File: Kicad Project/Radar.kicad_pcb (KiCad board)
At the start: 2 copper layers, 30 parts

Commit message: PCB Changes
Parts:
- added C12: C, Capacitors_SMD:C_0603, F.Cu at (160.2, 135.0)
- added C13: C, Capacitors_SMD:C_0603, F.Cu at (160.2, 140.0)
- added C14: C, Capacitors_SMD:C_0603, F.Cu at (163.5, 135.0)
- added R15: R, Resistors_SMD:R_0603, F.Cu at (163.5, 140.0)
- added U1: GALI-1+, RadarComponents:Amplifier, F.Cu at (150.4, 155.2)
- added U10: GALI-2+, RadarComponents:Amplifier, F.Cu at (150.9, 139.6)
- added U6: GALI-2+, RadarComponents:Amplifier, F.Cu at (112.1, 93.8)
- added U8: GALI-2+, RadarComponents:Amplifier, F.Cu at (152.9, 93.5)
- moved R7 68.9 mm to (117.9, 90.8), turned to 90 degrees
- moved .1uF1 67.1 mm to (105.7, 92.6), turned to 180 degrees
- moved R8 64.7 mm to (118.0, 84.6), turned to 270 degrees
- moved R10 54.5 mm to (128.3, 96.6), turned to 270 degrees
- moved C8 54.3 mm to (118.6, 88.1), turned to 180 degrees
- moved R9 51.9 mm to (125.3, 92.6), turned to 180 degrees
- moved C4 50.0 mm to (242.7, 113.1)
- moved R6 50.0 mm to (256.7, 113.0)
- moved C1 50.0 mm to (252.7, 113.1)
- moved C6 50.0 mm to (219.9, 118.1)
- moved C7 50.0 mm to (211.7, 113.1)
- moved R150 50.0 mm to (217.9, 131.8)
- moved R4 50.0 mm to (246.8, 118.1)
- moved R5 50.0 mm to (250.4, 118.1)
- moved C10 50.0 mm to (214.2, 131.8)
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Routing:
- added copper zone on F.Cu, net (none)
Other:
- board outline added: 104.1 x 101.6 mm

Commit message: PCB and Schematic updates
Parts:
- added R16: 75, RadarComponents:100PAD, F.Cu at (240.7, 109.0)
- added R17: 75, RadarComponents:100PAD, F.Cu at (227.9, 123.2)
- added R18: 75, RadarComponents:100PAD, F.Cu at (237.4, 114.1)
- added R19: 75, RadarComponents:100PAD, F.Cu at (220.7, 121.1)
- added U2: MCA1-85L+, RadarComponents:DZ885, F.Cu at (140.9, 118.0)
- added U3: LMV751, RadarComponents:SOT23-5, F.Cu at (125.8, 112.8)
- added U4: LMV751, RadarComponents:SOT23-5, F.Cu at (112.8, 111.1)
- added U5: LMV751, RadarComponents:SOT23-5, F.Cu at (103.9, 111.7)
- added U7: RMK-3-93+, RadarComponents:TT1224, F.Cu at (135.4, 93.4)
- added U9: LEE-39+, RadarComponents:Amplifier, F.Cu at (227.9, 113.7)
- .1uF1, .1uF2, .1uF3, .1uF4, C1, C10, C11, C12, C13, C14, C2, C3, C4, C5, C6, C7, C8, C9: footprint Capacitors_SMD:C_0603 -> RadarComponents:100PAD
- R1, R10, R11, R12, R13, R14, R15, R2, R7, R8, R9: footprint Resistors_SMD:R_0603 -> RadarComponents:100PAD
- moved R6 151.6 mm to (105.2, 117.2)
- moved R5 136.7 mm to (113.7, 117.4)
- moved R4 125.4 mm to (121.5, 112.9)
- moved C4 107.9 mm to (134.8, 111.2), turned to 90 degrees
- moved R3 98.3 mm to (132.1, 118.5)
- moved C1 84.4 mm to (168.3, 111.4), turned to 90 degrees
- moved R2 73.6 mm to (147.3, 105.4), turned to 0 degrees
- moved C3 71.0 mm to (148.6, 115.4), turned to 0 degrees
- moved C2 70.6 mm to (146.8, 109.5), turned to 0 degrees
- moved R1 64.1 mm to (152.8, 112.3)
- moved U1 41.8 mm to (160.3, 114.6), turned to 180 degrees
- moved C11 36.8 mm to (235.7, 104.7)
- moved C7 32.8 mm to (237.4, 133.4)
- moved C5 27.2 mm to (223.2, 137.3)
- moved R150 23.6 mm to (237.9, 119.1)
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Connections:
- net Net-(.1uF4-Pad1) renamed /SourceModule.sch/PowerSplitter
- net Net-(C10-Pad2) renamed /TXRX Module/receive_out
- net Net-(C11-Pad2) renamed /TXRX Module/transmit_in
- C12 pad 1: Net-(C12-Pad1) -> GND
- C13 pad 2: Net-(C13-Pad2) -> GND
- R1 pad 2: Net-(R1-Pad2) -> Net-(C3-Pad2)
- U10 pad 1: Net-(U10-Pad1) -> Net-(C11-Pad1)
- U10 pad 2: Net-(U10-Pad2) -> GND
- U10 pad 3: Net-(U10-Pad3) -> Net-(C14-Pad2)
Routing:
- added copper zone on F.Cu, net /SourceModule.sch/PowerSplitter
- removed copper zone on F.Cu, net (none)

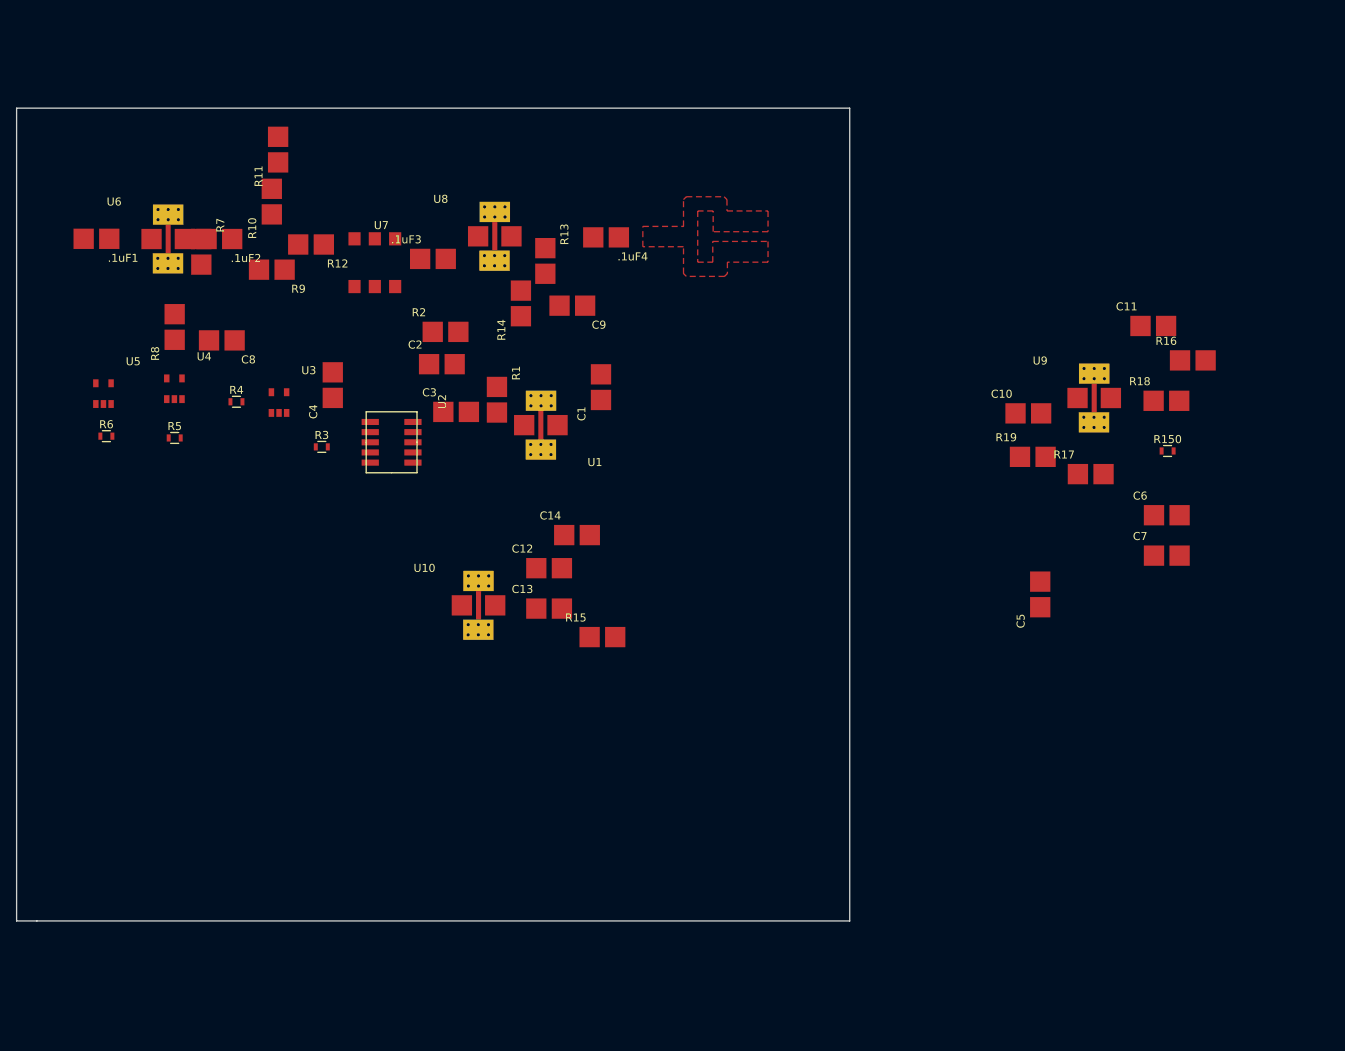
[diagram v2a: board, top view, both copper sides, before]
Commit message: PCB for source Module mostly complete, missing filter. Power Spliter still has issues.
Some minor changes made to all schematics for the net lists to be properall connected

A bunch of parts made
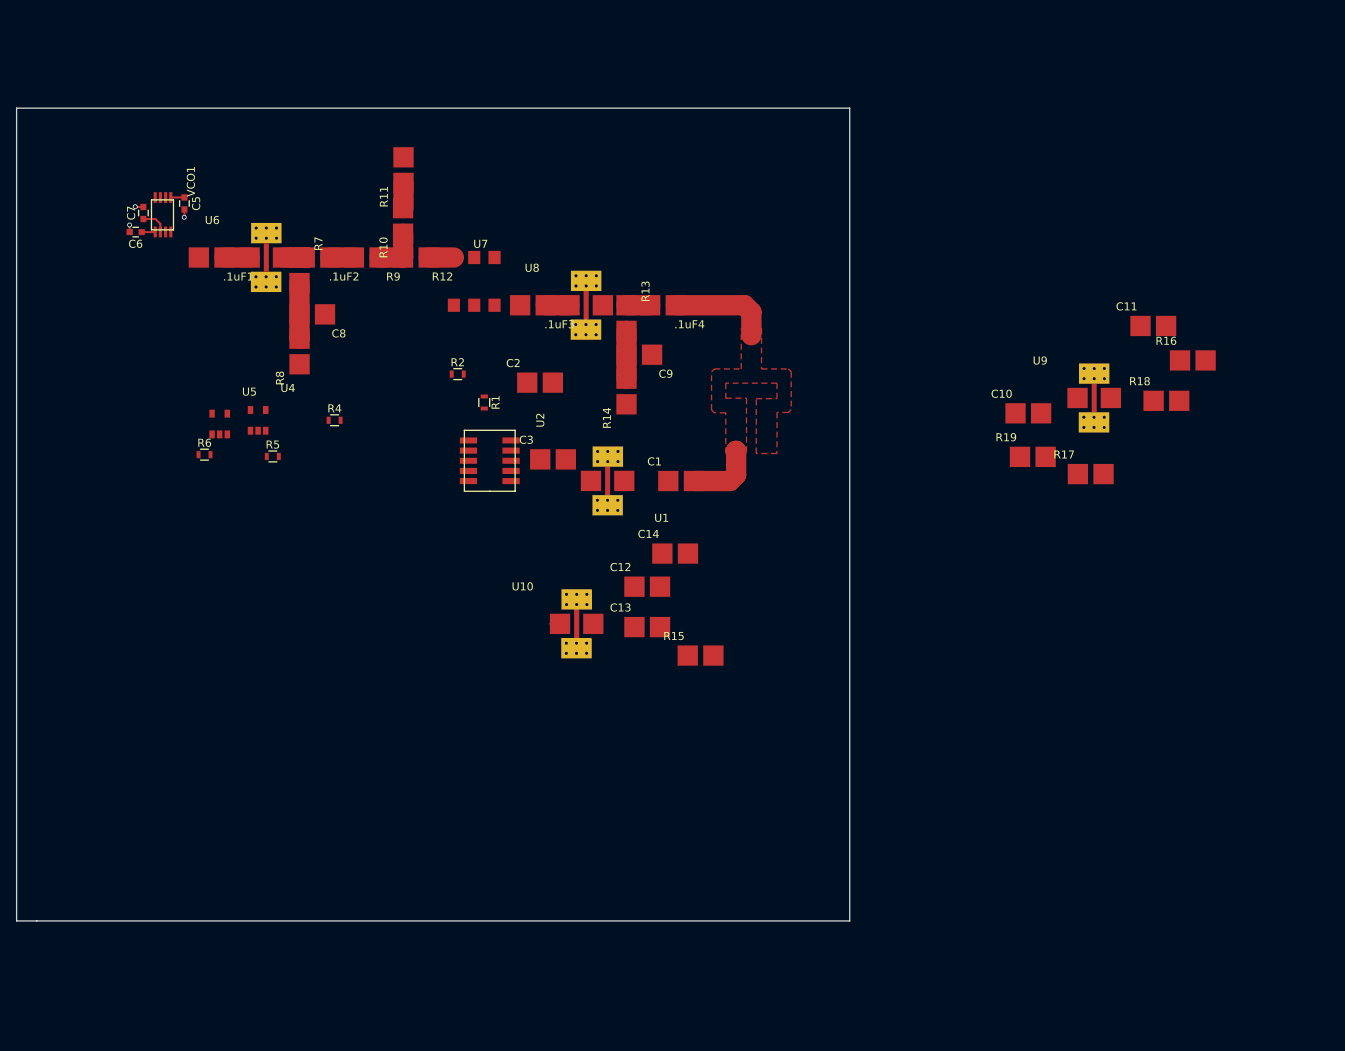
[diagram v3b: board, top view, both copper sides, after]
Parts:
- removed C4: 270pF, RadarComponents:100PAD
- removed R150: R, Resistors_SMD:R_0603
- removed R3: 390k, Resistors_SMD:R_0603
- removed U3: LMV751, RadarComponents:SOT23-5
- added VCO1: MAX2752, RadarComponents:MAX2752, F.Cu at (112.1, 88.2)
- C5, C6, C7: footprint RadarComponents:100PAD -> Capacitors_SMD:C_0603
- R1, R2: footprint RadarComponents:100PAD -> Resistors_SMD:R_0603
- moved C7 135.0 mm to (109.8, 89.3), turned to 90 degrees
- moved C6 133.7 mm to (108.9, 91.7), turned to 180 degrees
- moved C5 118.9 mm to (115.0, 88.1), turned to 270 degrees
- moved R14 17.2 mm to (171.5, 112.0)
- moved R10 16.6 mm to (143.6, 90.6)
- moved R8 15.9 mm to (130.6, 106.9)
- moved R11 15.9 mm to (143.6, 84.3)
- moved C1 15.2 mm to (176.7, 124.1), turned to 0 degrees
- moved U5 15.0 mm to (118.4, 115.5)
- moved .1uF1 14.6 mm to (118.7, 93.6)
- moved U8 14.3 mm to (164.4, 102.1)
- moved .1uF3 13.6 mm to (158.9, 99.6), turned to 180 degrees
- moved C3 13.5 mm to (160.7, 121.4)
- moved R12 13.2 mm to (144.2, 93.6)
- moved U7 12.6 mm to (147.9, 95.7)
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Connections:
- .1uF4 pad 1: /SourceModule.sch/PowerSplitter -> /DownconverterPreampModule/LO
- C1 pad 2: Net-(C1-Pad2) -> /DownconverterPreampModule/LO
- C10 pad 2: /TXRX Module/receive_out -> /DownconverterPreampModule/RFIN
- C11 pad 2: /TXRX Module/transmit_in -> /DownconverterPreampModule/LO
- R1 pad 2: Net-(C3-Pad2) -> Net-(R1-Pad2)
- R13 pad 2: Net-(R13-Pad2) -> Net-(C9-Pad2)
- R14 pad 2: Net-(R13-Pad2) -> Net-(C9-Pad2)
- U2 pad 3: Net-(R3-Pad2) -> Net-(R4-Pad2)
- U2 pad 5: Net-(U2-Pad5) -> /DownconverterPreampModule/RFIN
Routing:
- net /DownconverterPreampModule/LO: track 0.00 -> 21.3 mm
- net Net-(C8-Pad2): track 0.00 -> 6.95 mm
- net Net-(C9-Pad2): track 0.00 -> 5.98 mm
- net Net-(R10-Pad1): track 0.00 -> 5.92 mm
- net +3V3: track 0.00 -> 5.09 mm
- net GND: track 0.00 -> 3.25 mm, vias 0 -> 3
- net Net-(R12-Pad1): track 0.00 -> 3.15 mm
- net Net-(.1uF1-Pad1): track 0.00 -> 3.15 mm
- net Net-(R10-Pad2): track 0.00 -> 3.10 mm
- net Net-(.1uF3-Pad1): track 0.00 -> 2.97 mm
- net Net-(.1uF4-Pad2): track 0.00 -> 2.96 mm
- net Net-(.1uF2-Pad1): track 0.00 -> 2.95 mm
- net Net-(.1uF2-Pad2): track 0.00 -> 2.72 mm
- net Net-(C5-Pad1): track 0.00 -> 1.71 mm
- net Net-(C11-Pad1): track 0.00 -> 1.23 mm

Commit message: PCB LAYOUT update
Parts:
- added MS1: PowerDivider, RadarComponents:powersplitter2, F.Cu at (183.6, 113.6)
- C10, C11, C12, C13, C14: value C -> 150p
- R1, R2: footprint Resistors_SMD:R_0603 -> RadarComponents:100PAD
- moved R16 114.5 mm to (132.3, 145.9)
- moved C10 114.5 mm to (111.8, 152.6)
- moved R17 114.5 mm to (119.6, 160.1)
- moved R19 114.5 mm to (112.3, 158.0)
- moved U9 114.5 mm to (119.5, 150.6)
- moved R18 114.5 mm to (129.0, 151.0)
- moved C11 54.4 mm to (188.5, 131.7), turned to 90 degrees
- moved C2 11.2 mm to (147.9, 110.5)
- moved .1uF2 8.31 mm to (123.6, 93.6)
- moved C5 8.31 mm to (106.7, 88.1)
- moved C6 8.31 mm to (100.6, 91.7)
- moved C7 8.31 mm to (101.5, 89.3)
- moved C8 8.31 mm to (123.0, 100.7)
- moved R10 8.31 mm to (135.3, 90.6)
- moved R11 8.31 mm to (135.3, 84.3)
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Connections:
- net /DownconverterPreampModule/RFIN renamed RFIN
- .1uF3 pad 2: Net-(.1uF3-Pad2) -> GND
- .1uF4 pad 1: /DownconverterPreampModule/LO -> Net-(.1uF4-Pad1)
- C1 pad 2: /DownconverterPreampModule/LO -> PowerSplitter
- C11 pad 2: /DownconverterPreampModule/LO -> PowerSplitter
- R1 pad 2: Net-(R1-Pad2) -> Net-(C3-Pad2)
- R17 pad 2: Net-(R17-Pad2) -> +9V
- R19 pad 1: Net-(R19-Pad1) -> +9V
- U7 pad 4: Net-(.1uF3-Pad2) -> GND
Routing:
- net /DownconverterPreampModule/LO: track 21.3 -> 0.00 mm
- net GND: track 3.25 -> 23.6 mm, vias 3 -> 6
- net Net-(.1uF4-Pad1): track 0.00 -> 11.5 mm
- net PowerSplitter: track 0.00 -> 8.05 mm
- net Net-(.1uF1-Pad2): track 0.00 -> 4.67 mm
- added copper zone on B.Cu, net GND
- added copper zone on F.Cu, net GND
- added copper zone on F.Cu, net Net-(.1uF2-Pad2)
